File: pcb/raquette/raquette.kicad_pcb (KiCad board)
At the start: 2 copper layers, 105 x 165 mm, 17 parts, among them U1 Teensy 4.1

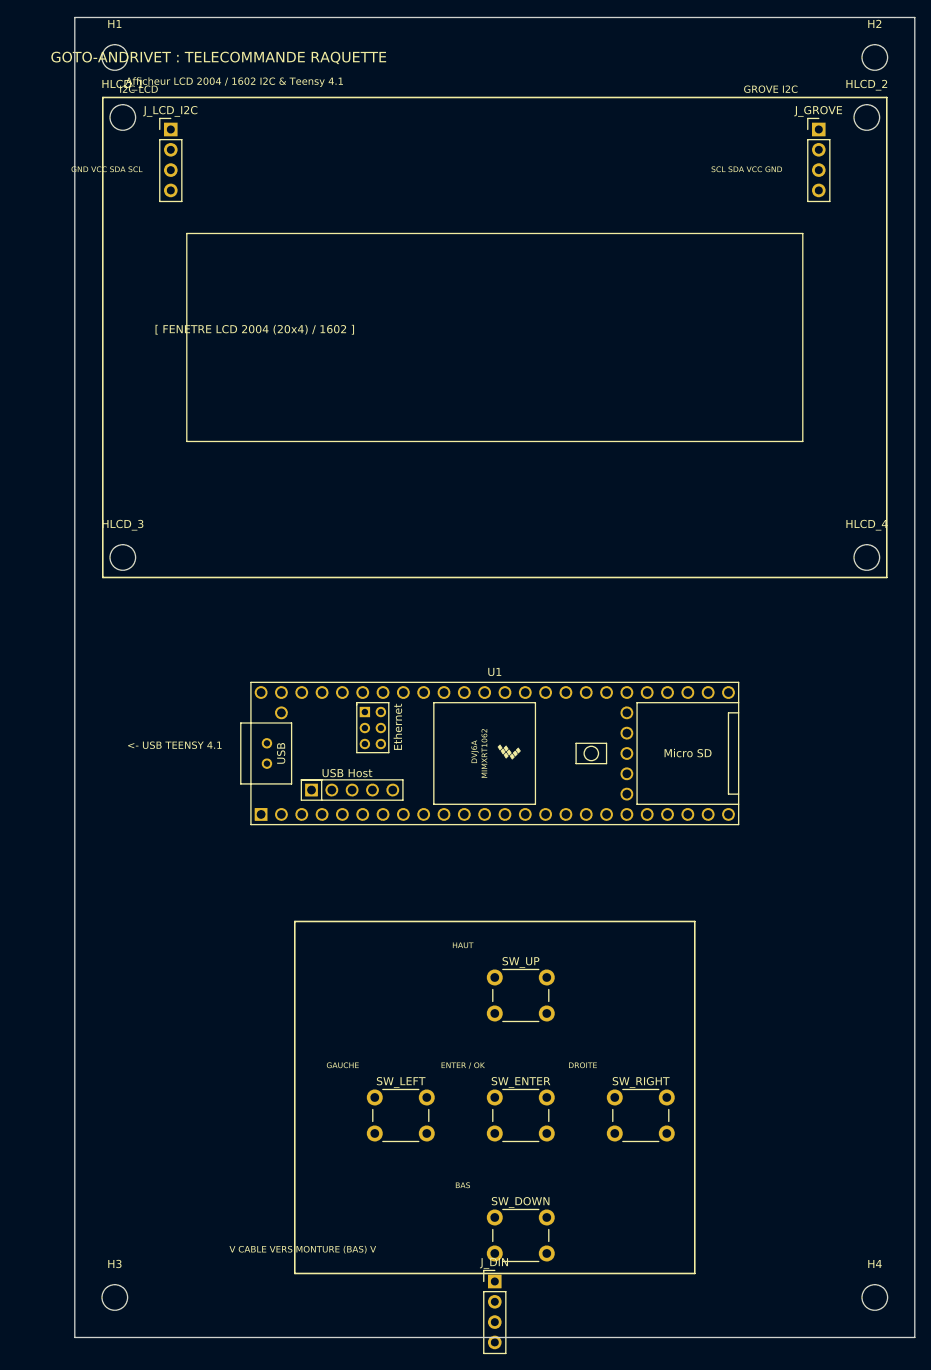
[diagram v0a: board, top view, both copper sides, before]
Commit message: PCB Raquette: Optimisation de la taille (-20mm), rotation du Teensy a l'horizontale et rotation du connecteur DIN vers le bas
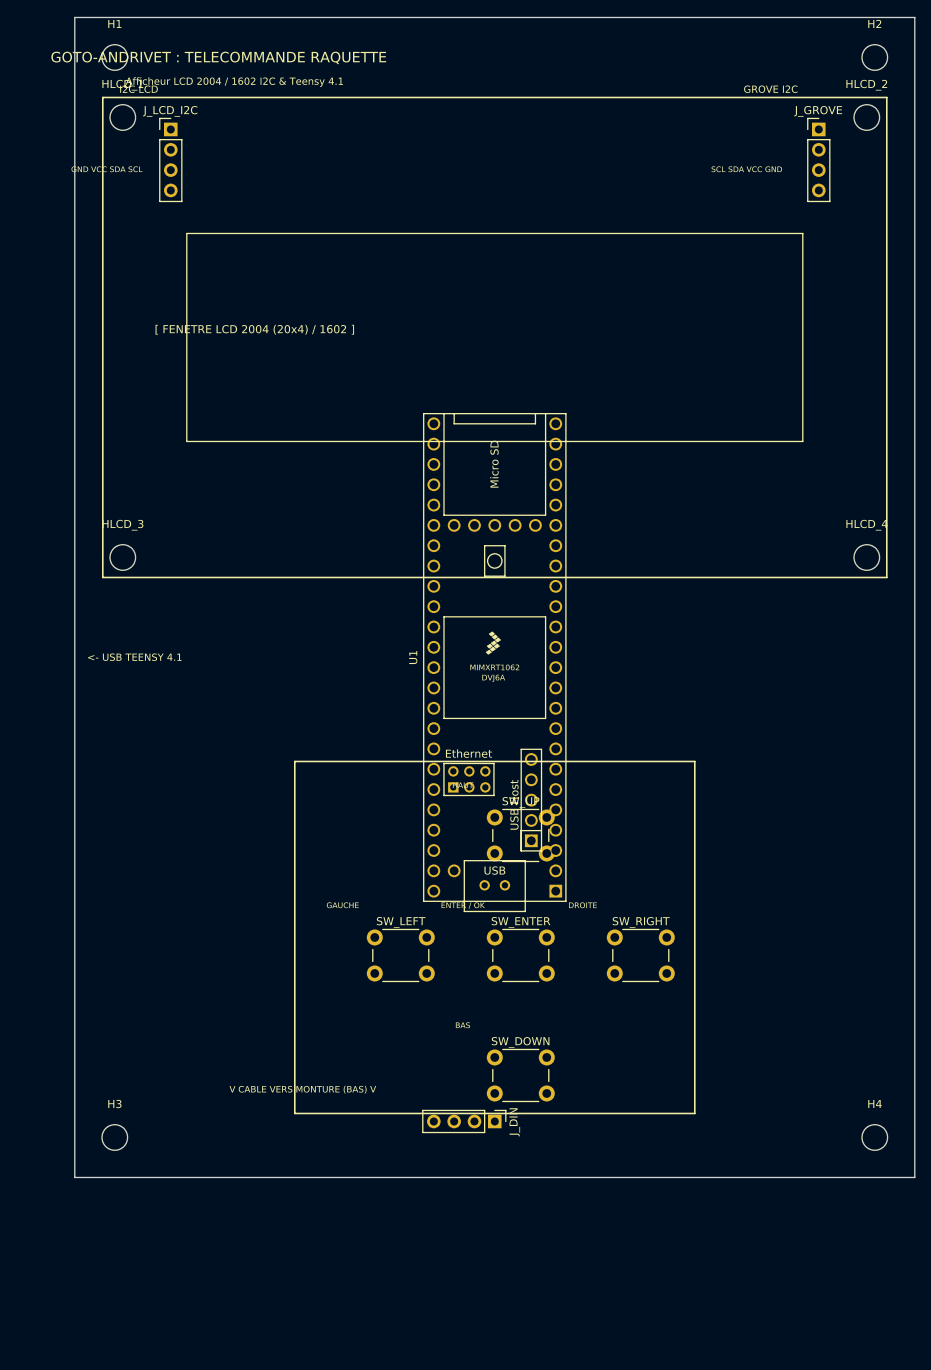
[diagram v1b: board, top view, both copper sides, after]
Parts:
- moved H3 20.0 mm to (5.00, 140.0)
- moved H4 20.0 mm to (100.0, 140.0)
- moved J_DIN 20.0 mm to (52.5, 138.0), turned to -90 degrees
- moved SW_DOWN 20.0 mm to (52.5, 130.0)
- moved SW_ENTER 20.0 mm to (52.5, 115.0)
- moved SW_LEFT 20.0 mm to (37.5, 115.0)
- moved SW_RIGHT 20.0 mm to (67.5, 115.0)
- moved SW_UP 20.0 mm to (52.5, 100.0)
- moved U1 12.0 mm to (52.5, 80.0), turned to 90 degrees
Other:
- board size 105 x 165 mm -> 105 x 145 mm

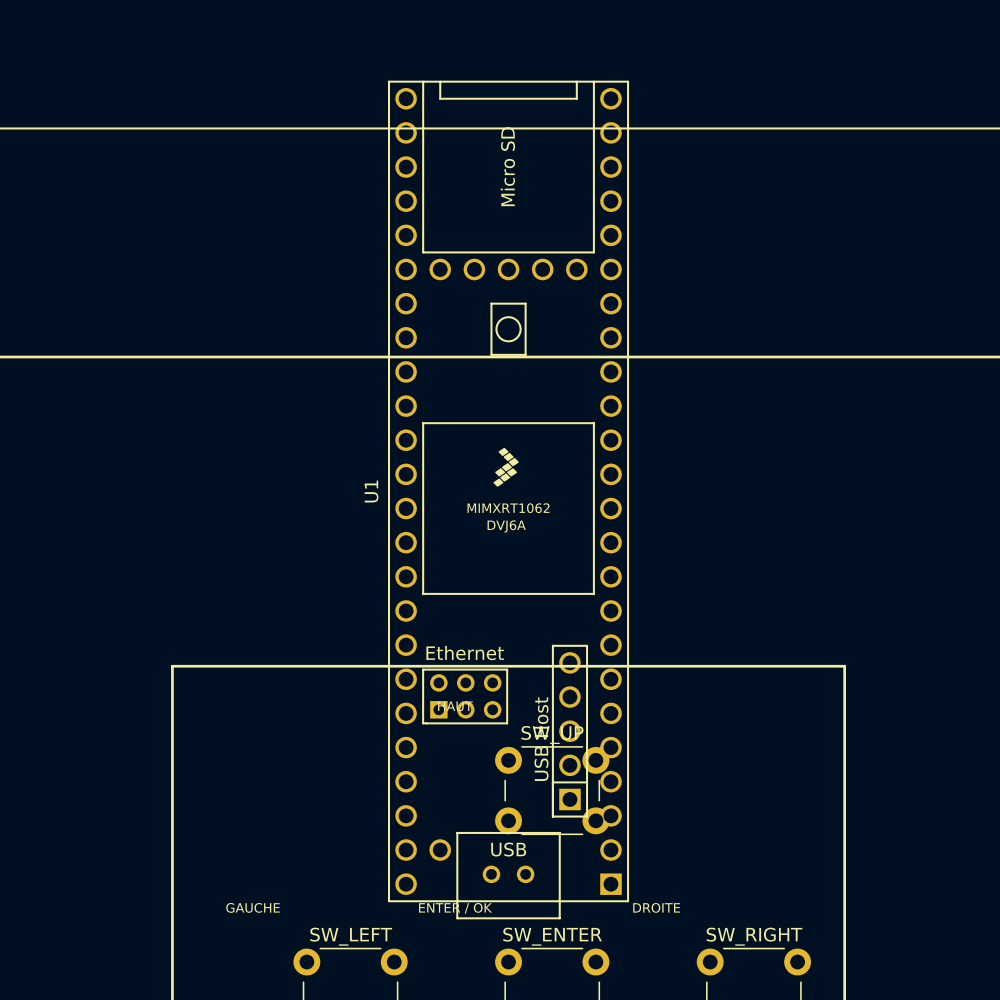
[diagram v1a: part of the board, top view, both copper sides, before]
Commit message: PCB Raquette: Fix chevauchement (Teensy etait vertical a cause du SetOrientationDegrees90)
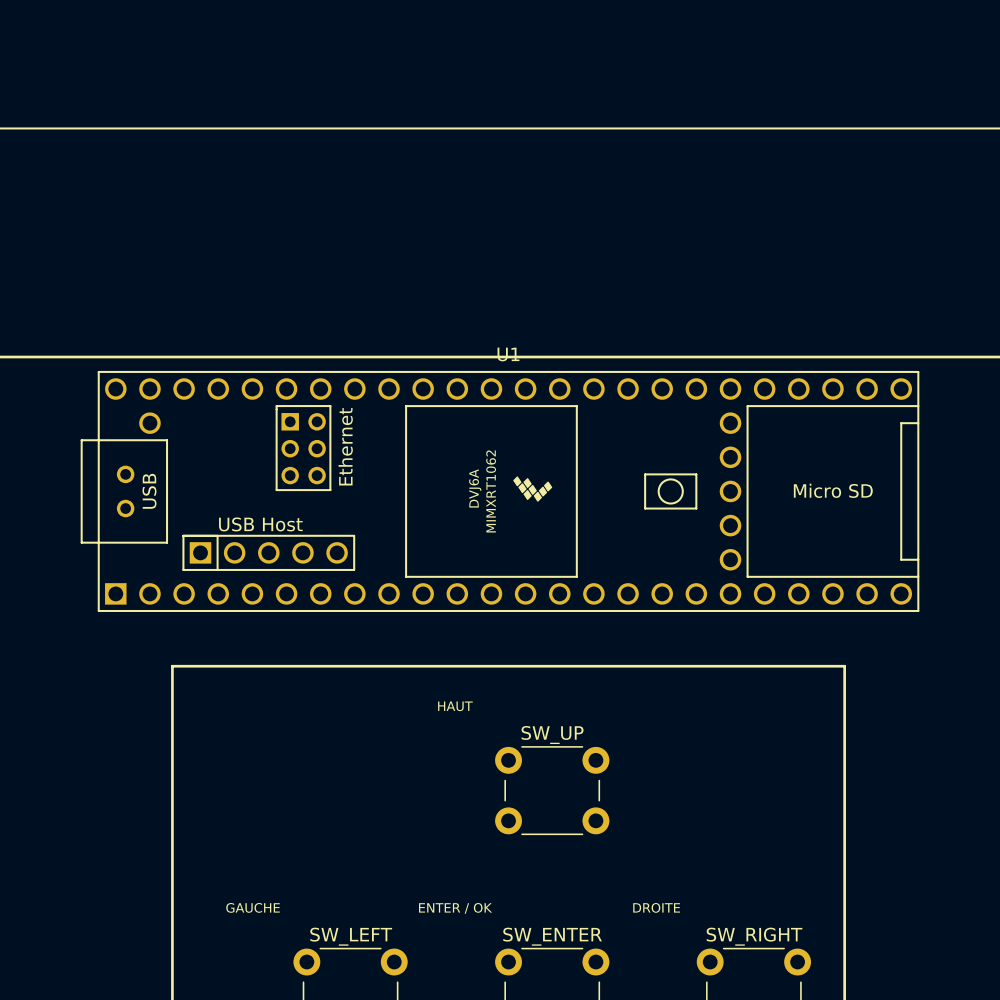
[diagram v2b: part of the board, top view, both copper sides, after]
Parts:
- turned U1 to 0 degrees

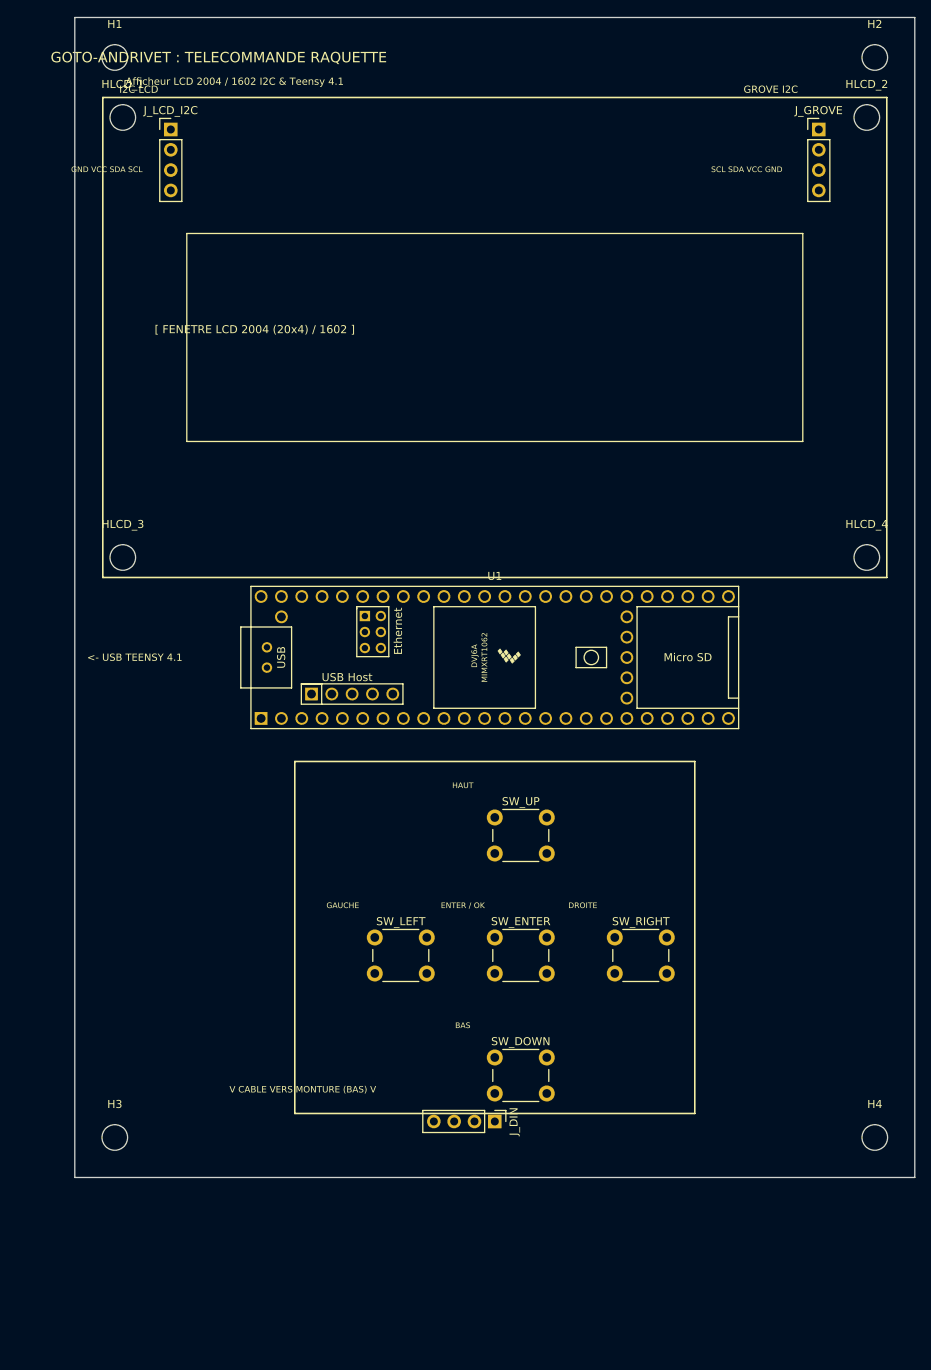
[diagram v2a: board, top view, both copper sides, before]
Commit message: PCB Raquette: Ajustement vertical (+5mm d'espace) pour eloigner les pins du Teensy de l'ecran LCD
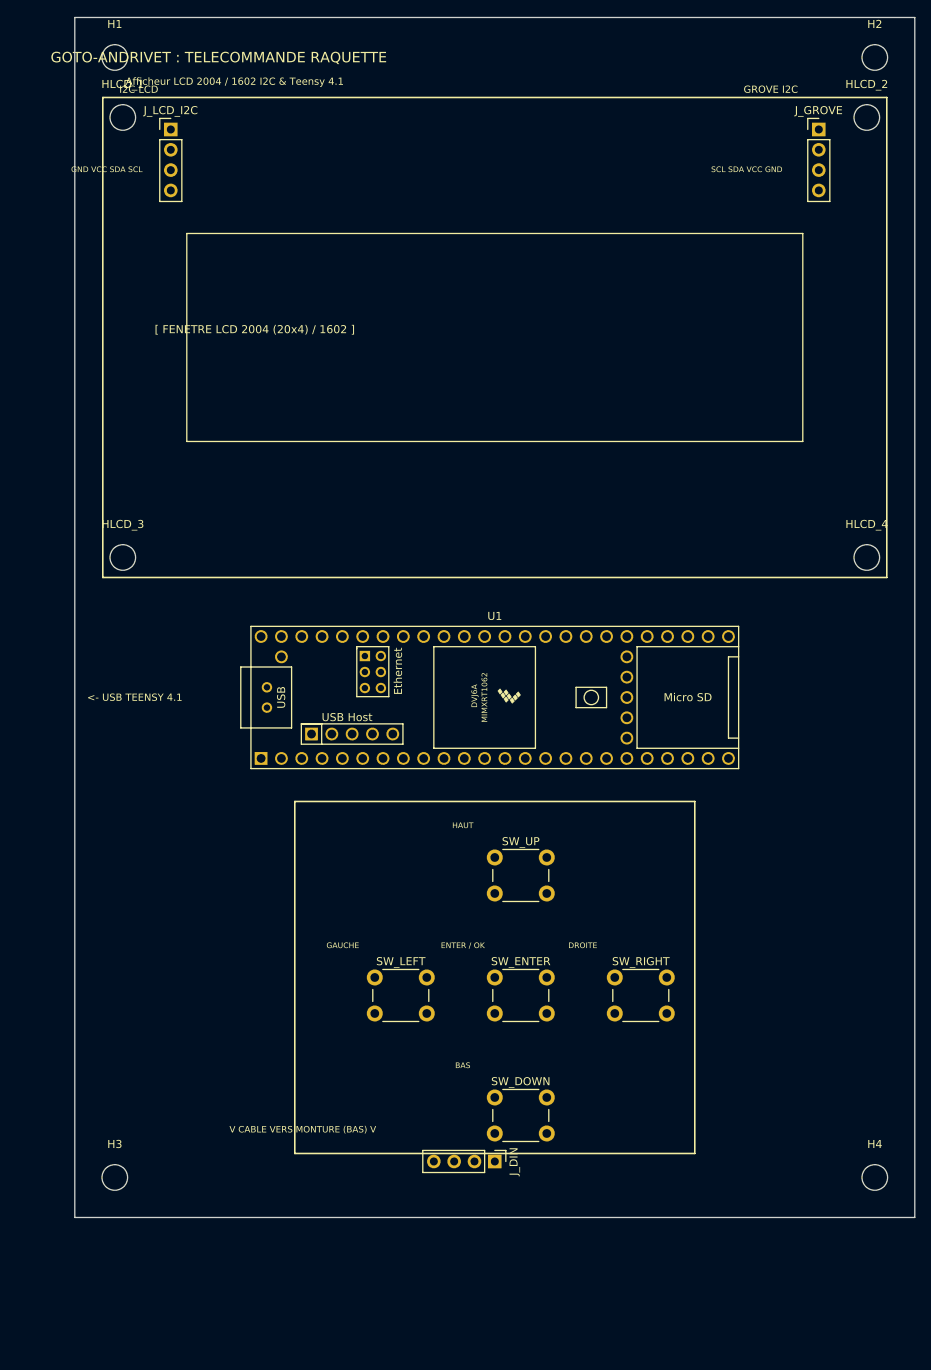
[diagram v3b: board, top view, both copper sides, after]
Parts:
- moved H3 5.00 mm to (5.00, 145.0)
- moved H4 5.00 mm to (100.0, 145.0)
- moved J_DIN 5.00 mm to (52.5, 143.0)
- moved SW_DOWN 5.00 mm to (52.5, 135.0)
- moved SW_ENTER 5.00 mm to (52.5, 120.0)
- moved SW_LEFT 5.00 mm to (37.5, 120.0)
- moved SW_RIGHT 5.00 mm to (67.5, 120.0)
- moved SW_UP 5.00 mm to (52.5, 105.0)
- moved U1 5.00 mm to (52.5, 85.0)
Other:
- board size 105 x 145 mm -> 105 x 150 mm

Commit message: PCB Raquette: deplacement des ports I2C sous l'ecran et remplacement du connecteur DIN par de gros pads pour souder des fils directs
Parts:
- removed the J_DIN at (52.5, 143.0)
- added J_DIN: CABLE MONTURE, SolderWire-0.5sqmm_1x04_P4.8mm_D0.9mm_OD2.3mm, F.Cu at (45.3, 143.0)
- moved J_GROVE 71.0 mm to (93.0, 85.0)
- moved J_LCD_I2C 71.0 mm to (12.0, 85.0)

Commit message: PCB Raquette: Fix orientation des SolderPads (par defaut horizontal) et ajout de la serigraphie du pinout
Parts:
- turned J_DIN to 0 degrees
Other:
- board text added: "1:GND 2:+5V 3:TX 4:RX"

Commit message: PCB Raquette: descente des connecteurs I2C a Y=100 pour degager l'acces au port micro-USB du Teensy
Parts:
- moved J_GROVE 15.0 mm to (93.0, 100.0)
- moved J_LCD_I2C 15.0 mm to (12.0, 100.0)

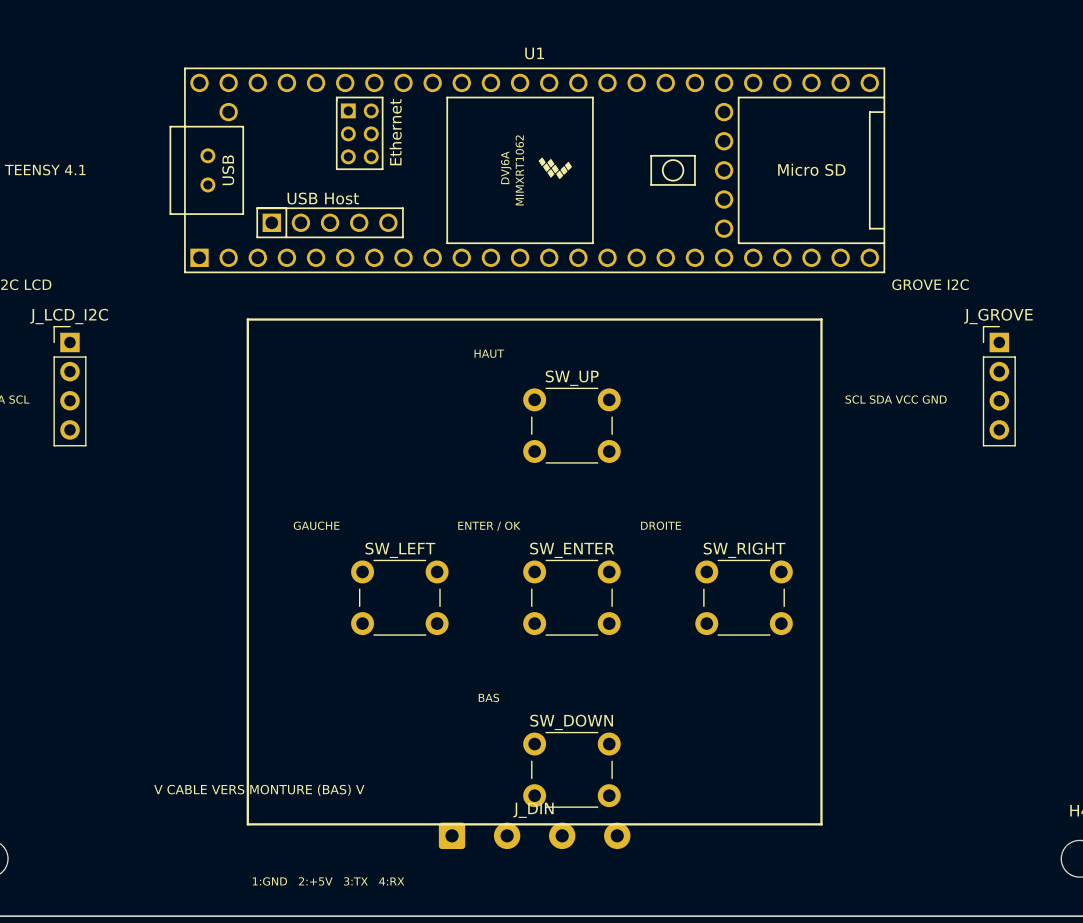
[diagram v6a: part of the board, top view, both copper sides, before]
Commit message: Auto-routing: tracé des pistes (avec classe Puissance 0.8mm pour la monture) et correction DRC
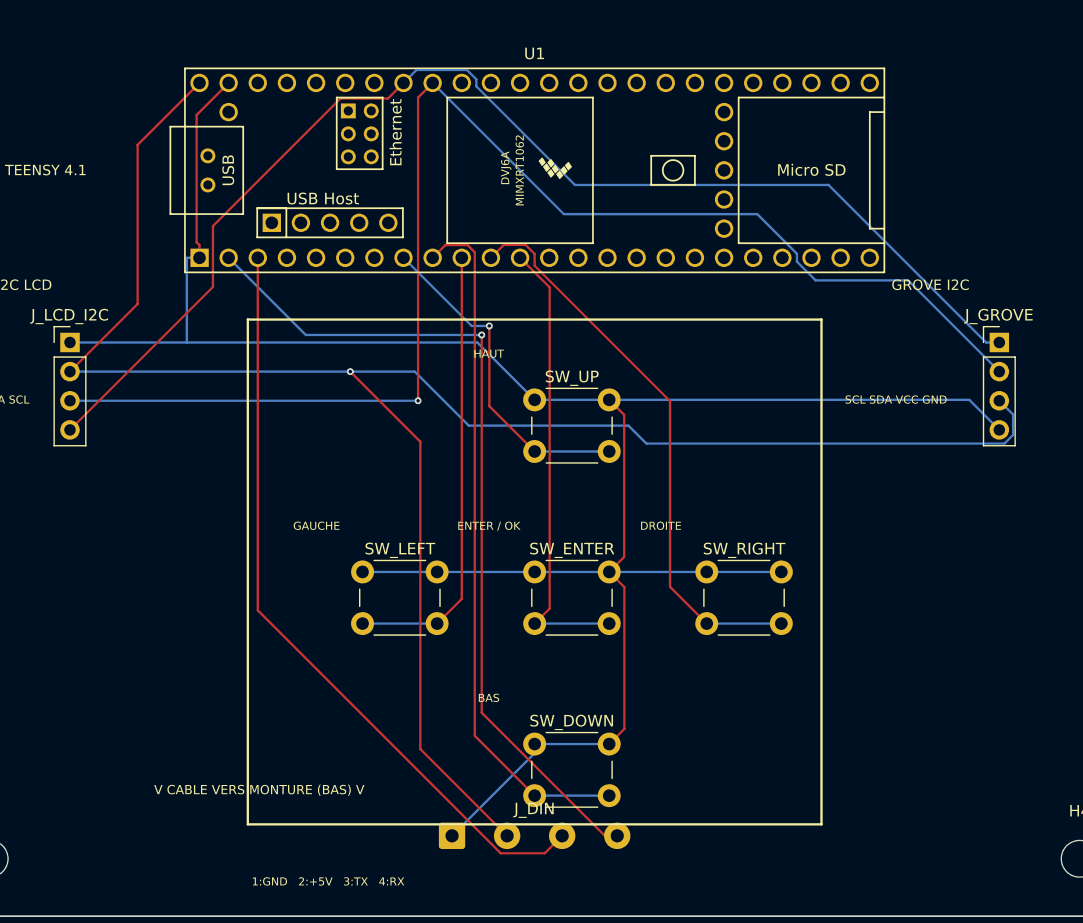
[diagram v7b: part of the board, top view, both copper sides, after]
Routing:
- net GND: track 0.00 -> 195.3 mm
- net +5V: track 0.00 -> 164.5 mm, vias 0 -> 1
- net I2C_SDA: track 0.00 -> 118.8 mm, vias 0 -> 1
- net I2C_SCL: track 0.00 -> 107.3 mm
- net RAQ_RX: track 0.00 -> 74.0 mm, vias 0 -> 1
- net RAQ_TX: track 0.00 -> 66.7 mm
- net BTN_DOWN: track 0.00 -> 60.4 mm
- net BTN_RIGHT: track 0.00 -> 49.5 mm
- net BTN_ENTER: track 0.00 -> 40.0 mm
- net BTN_LEFT: track 0.00 -> 39.3 mm
- net BTN_UP: track 0.00 -> 29.0 mm, vias 0 -> 1
